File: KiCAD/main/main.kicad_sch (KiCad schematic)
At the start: 49 parts, among them J1 USB_C_Receptacle_USB2.0_14P, J2 Conn_Coaxial, J3 Conn_01x07_Socket, SW1 SW_SPDT, U1 SX1262IMLTRT, U2 TP4056-42-ESOP8, U3 BGS12P2L, U4 ESP32-S3-MINI-1, U6 MIC5219-3.3YMM, U7 CH340X

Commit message: added a huge schematic overhaul
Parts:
- removed H1, H2: MountingHole_Pad, MountingHole:MountingHole_2.2mm_M2_DIN965_Pad_TopBottom, symbol Mechanical:MountingHole_Pad
- removed TP5, TP6, TP7, TP8: TestPoint, TestPoint:TestPoint_Pad_1.5x1.5mm, symbol Connector:TestPoint
- added C8: 0.1uF, symbol Device:C
- added D3: WS2812B, LED_SMD:LED_WS2812B_PLCC4_5.0x5.0mm_P3.2mm, symbol LED:WS2812B
- added J4: Micro_SD_Card, customlib:SIM-SMD_8P-1040310811, symbol Connector:Micro_SD_Card
- added R11, R12, R13, R14, R15, R16, R17, R3, R6, R8: 10K, Resistor_SMD:R_0603_1608Metric, symbol Device:R
- added R18: R, symbol Device:R
- added SW2, SW3, SW4, SW5, SW6: SW_Push, customlib:SW-SMD_4P-L3.5-W3.0-P1.50-LS4.7, symbol Switch:SW_Push
- C1, C2: LCSC Part # C15849 -> C77386
- R10, R4, R9: LCSC Part # C25804 -> C2961367
- U4: LCSC Part # (none) -> C2913206
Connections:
- net GND: now also C8.1, D3.3 (VSS), J4.6 (VSS), J4.SH (SHIELD), SW2.2, SW3.2, SW4.2, SW5.2, SW6.2
- net VCC: now also C8.2, J4.4 (VDD), R11.2, R12.2, R13.1, R14.1, R15.1, R16.1, R17.1, R3.2, R6.2, R8.2, SW2.1, SW3.1, SW4.1, SW5.1, SW6.1
- net UP: now reaches U4.12 (IO8)
- net UP: now also R3.1
- net RIGHT: now reaches U4.13 (IO9)
- net RIGHT: now also R6.1
- net SEL: now reaches U4.14 (IO10)
- net SEL: now also R8.1
- net LEFT: now reaches U4.15 (IO11)
- net LEFT: now also R11.1
- net DOWN: now reaches U4.16 (IO12)
- net DOWN: now also R12.1
- net NEOPXL_D: now reaches U4.17 (IO13)
- net NEOPXL_D: now also R18.2
- net 5V: now reaches C1.2, SW1.1 (A), U6.1 (EN), U6.2 (IN)
- net 5V: now also D3.1 (VDD)
- new net: D3.4 (DIN), R18.1
- new net CLK: J4.5 (CLK)
- new net CMD: J4.3 (CMD), R15.2
- new net DAT0: J4.7 (DAT0), R14.2
- new net DAT1: J4.8 (DAT1), R13.2
- new net DAT2: J4.1 (DAT2), R16.2
- new net DAT3/CD: J4.2 (DAT3/CD), R17.2
- no-connect marks 9 -> 10
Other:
- note added: "DPAD"
- note added: "JTAG Probing Points"
- note added: "LiPo Charging"
- note added: "LoRa Radio Interface"
- note added: "MCU"
- note added: "Main USB Connection (USB-C)"
- note added: "Neopixel"
- note added: "Power Supply"
- note added: "SPI Display connector"
- note added: "Sheet Annotations"
- note added: "Storage"
- note added: "USB to Serial Bridge"
- note removed: "DNP"
- moved on the sheet: BT1, C1, C10, C11, C12, C13, C14, C15, C16, C17, C18, C2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

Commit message: Rev 3 done!
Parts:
- removed R10, R8, R9: 10K, Resistor_SMD:R_0603_1608Metric, symbol Device:R
- removed SW2, SW3, SW5, SW6: SW_Push, customlib:SW-SMD_4P-L3.5-W3.0-P1.50-LS4.7, symbol Switch:SW_Push
- added C19, C20, C9: 0.1uF, Capacitor_SMD:C_0402_1005Metric, symbol Device:C
- added SW2: RotaryEncoder, customlib:HYCW01-4D-4P-DZ, symbol Device:RotaryEncoder
- C8: footprint (none) -> Capacitor_SMD:C_0402_1005Metric; LCSC Part # (none) -> C1525
- D3: LCSC Part # (none) -> C114586
- FL1: LCSC Part # (none) -> C7434807; now in the parts list
- J3: now left out of the parts list
- J4: LCSC Part # (none) -> C585350
- R18: value R -> 450R; footprint (none) -> Resistor_SMD:R_0402_1005Metric; LCSC Part # (none) -> C186129
- SW4: footprint customlib:SW-SMD_4P-L3.5-W3.0-P1.50-LS4.7 -> customlib:SW-TH_3P-L5.8_WSGT-3P-CC; LCSC Part # C49393608 -> C22386787
- U4: now in the parts list
- renumbered TP3 to TCK1, TP1 to TDI1, TP2 to TDO1, TP4 to TMS1
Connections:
- net GND: now also SW4.1, C19.1, C20.2, C9.1, SW2.C; no longer SW4.2
- net NEOPXL_D: now also U4.44 (IO46); no longer U4.17 (IO13)
- net SEL: now also SW4.2, U4.16 (IO12), C20.1; no longer U4.14 (IO10)
- net VCC: no longer C10.1, C14.2, C17.2, C18.2, C2.2, C3.2, C4.2, C6.1, C7.1, C8.2, J4.4 (VDD), R11.2, R12.2, R13.1, R14.1, R15.1, R16.1, R17.1, R3.2, R4.1, R6.2, SW4.1, U1.1 (VDD_IN), U1.10 (VBAT), U1.11 (VBAT_IO), U3.4 (VDD), U4.3 (3V3), U6.3 (OUT), U7.10 (V3), U7.7 (VCC)
- net ~{CHRG}: now also R11.1, U4.32 (IO36); no longer U4.20 (IO16)
- net ~{STDBY}: now also R12.1, U4.31 (IO35); no longer U4.21 (IO17)
- net 5V renamed +5V
- removed net DOWN: R12.1, U4.16 (IO12)
- net LEFT renamed ENC_PHS_A
- net ENC_PHS_A: now also R6.1, C9.2, SW2.A; no longer R11.1
- net RIGHT renamed SCL
- net SCL: no longer R6.1
- net UP renamed ENC_PHS_B
- net ENC_PHS_B: now also U4.14 (IO10), C19.2, SW2.B; no longer U4.12 (IO8)
- new net +3.3V: C10.1, C14.2, C17.2, C18.2, C2.2, C3.2, C4.2, C6.1, C7.1, C8.2, J4.4 (VDD), R11.2, R12.2, R13.1, R14.1, R15.1, R16.1, R17.1, R3.2, R4.1, R6.2, U1.1 (VDD_IN), U1.10 (VBAT), U1.11 (VBAT_IO), U3.4 (VDD), U4.3 (3V3), U6.3 (OUT), U7.10 (V3), U7.7 (VCC)
- new net PWR: U4.17 (IO13)
- new net SDA: U4.12 (IO8)
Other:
- note added: "Dial"
- note added: "I2C"
- note removed: "DPAD"
- moved on the sheet: BT1, C1, C10, C11, C12, C13, C14, C15, C16, C17, C18, C2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

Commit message: Brushing off dust
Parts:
- removed C20: 0.1uF, Capacitor_SMD:C_0402_1005Metric, symbol Device:C
- removed SW4: SW_Push, customlib:SW-TH_3P-L5.8_WSGT-3P-CC, symbol Switch:SW_Push
- added H1, H2, H3, H4: MountingHole_Pad_MP, MountingHole:MountingHole_2.5mm_Pad_TopBottom, symbol Mechanical:MountingHole_Pad_MP
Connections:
- net GND: now also H1.MP, H2.MP, H3.MP, H4.MP
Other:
- note added: "Mounting"
- note removed: "I2C"
- moved on the sheet: C19, C9, R3, R6, SW2

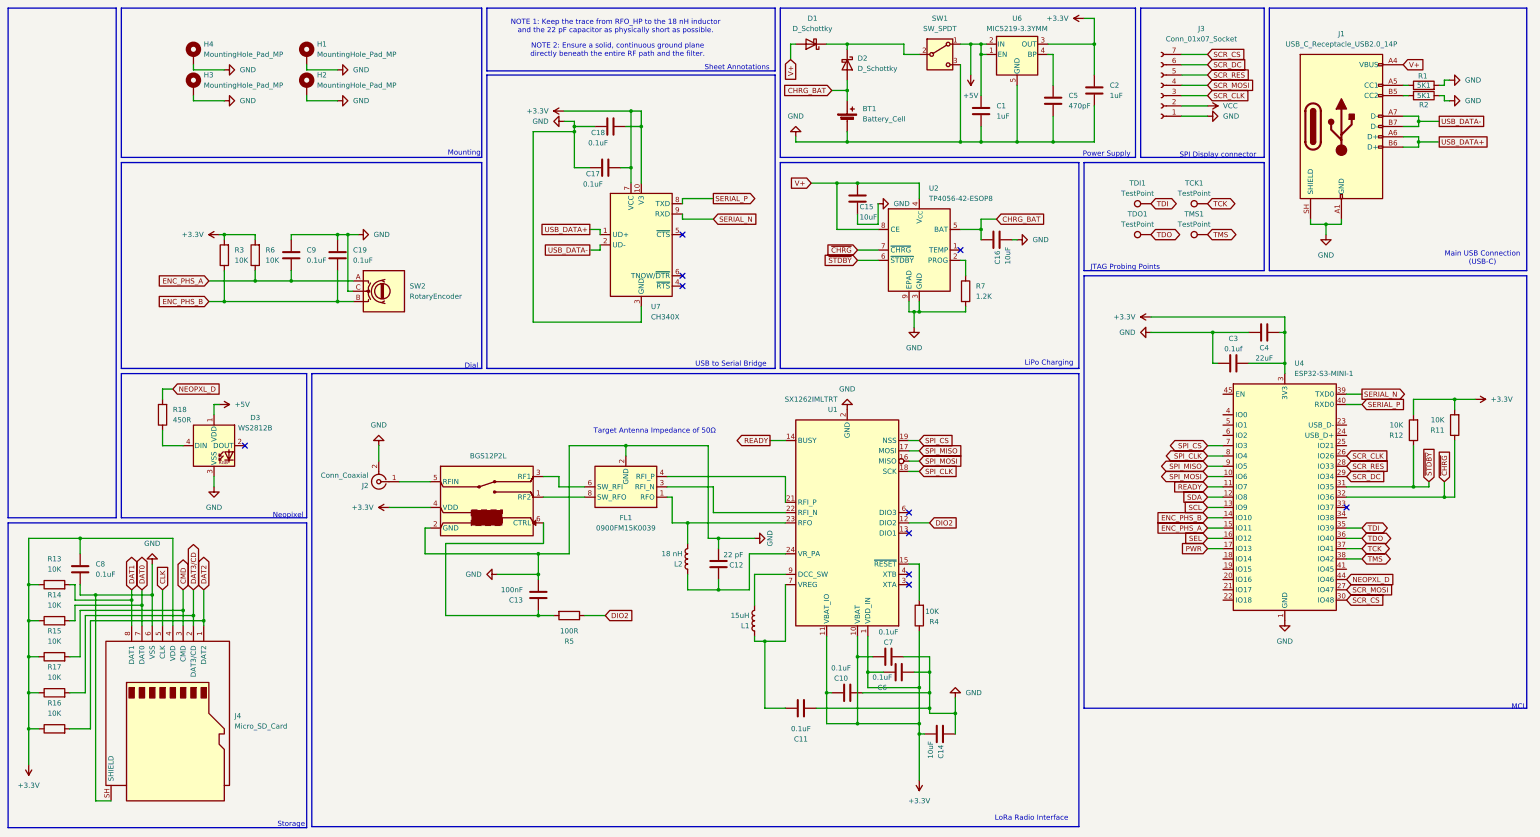
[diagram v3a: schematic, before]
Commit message: Replaced ESP-WROOM module with ESP32-S3 module for flexable usage and stocking
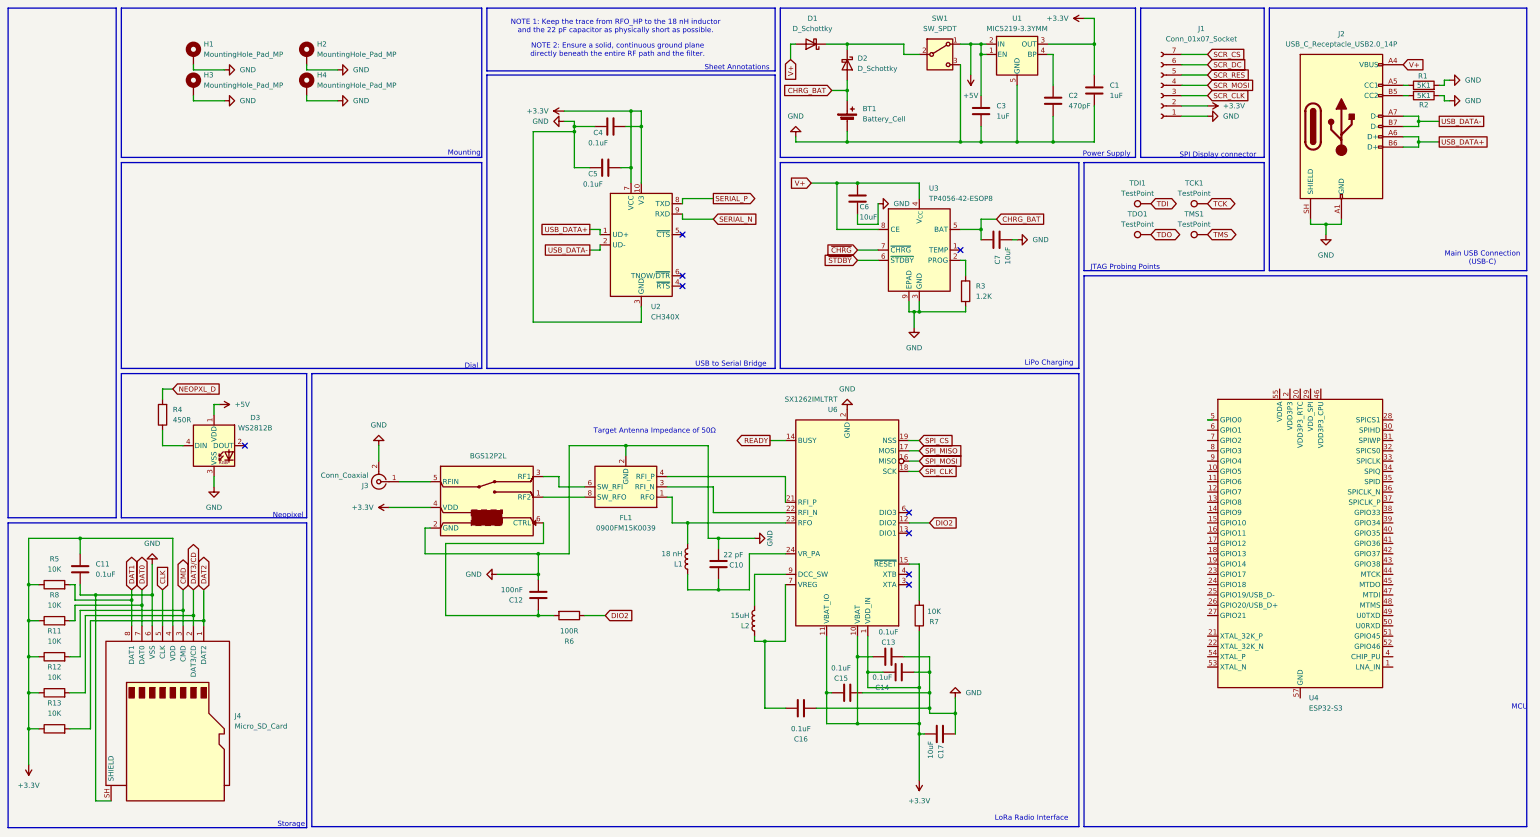
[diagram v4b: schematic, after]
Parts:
- removed C18, C19, C8, C9: 0.1uF, Capacitor_SMD:C_0402_1005Metric, symbol Device:C
- removed J1: USB_C_Receptacle_USB2.0_14P, Connector_USB:USB_C_Receptacle_GCT_USB4110, symbol Connector:USB_C_Receptacle_USB2.0_14P
- removed J2: Conn_Coaxial, Connector_Coaxial:SMA_Amphenol_132289_EdgeMount, symbol Connector:Conn_Coaxial
- removed J3: Conn_01x07_Socket, Connector_PinHeader_2.54mm:PinHeader_1x07_P2.54mm_Vertical, symbol Connector:Conn_01x07_Socket
- removed R14, R15, R16, R17: 10K, Resistor_SMD:R_0603_1608Metric, symbol Device:R
- removed R18: 450R, Resistor_SMD:R_0402_1005Metric, symbol Device:R
- removed SW2: RotaryEncoder, customlib:HYCW01-4D-4P-DZ, symbol Device:RotaryEncoder
- removed U1: SX1262IMLTRT, Package_DFN_QFN:QFN-24-1EP_4x4mm_P0.5mm_EP2.6x2.6mm, symbol RF:SX1262IMLTRT
- removed U2: TP4056-42-ESOP8, Package_SO:SOIC-8-1EP_3.9x4.9mm_P1.27mm_EP2.41x3.3mm_ThermalVias, symbol Battery_Management:TP4056-42-ESOP8
- removed U3: BGS12P2L, Package_LGA:Infineon_PG-TSNP-6-10_0.7x1.1mm_0.7x1.1mm_P0.4mm, symbol Personal:BGS12P2L
- removed U4: ESP32-S3-MINI-1, RF_Module:ESP32-S2-MINI-1, symbol RF_Module:ESP32-S3-MINI-1
- removed U6: MIC5219-3.3YMM, Package_SO:MSOP-8_3x3mm_P0.65mm, symbol Regulator_Linear:MIC5219-3.3YMM
- removed U7: CH340X, Package_SO:MSOP-10_3x3mm_P0.5mm, symbol Interface_USB:CH340X
- added J1: Conn_01x07_Socket, Connector_PinHeader_2.54mm:PinHeader_1x07_P2.54mm_Vertical, symbol Connector:Conn_01x07_Socket
- added J2: USB_C_Receptacle_USB2.0_14P, Connector_USB:USB_C_Receptacle_GCT_USB4110, symbol Connector:USB_C_Receptacle_USB2.0_14P
- added J3: Conn_Coaxial, Connector_Coaxial:SMA_Amphenol_132289_EdgeMount, symbol Connector:Conn_Coaxial
- added R8: 10K, Resistor_SMD:R_0603_1608Metric, symbol Device:R
- added U1: MIC5219-3.3YMM, Package_SO:MSOP-8_3x3mm_P0.65mm, symbol Regulator_Linear:MIC5219-3.3YMM
- added U2: CH340X, Package_SO:MSOP-10_3x3mm_P0.5mm, symbol Interface_USB:CH340X
- added U3: TP4056-42-ESOP8, Package_SO:SOIC-8-1EP_3.9x4.9mm_P1.27mm_EP2.41x3.3mm_ThermalVias, symbol Battery_Management:TP4056-42-ESOP8
- added U4: ESP32-S3, Package_DFN_QFN:QFN-56-1EP_7x7mm_P0.4mm_EP4x4mm, symbol MCU_Espressif:ESP32-S3
- added U5: BGS12P2L, Package_LGA:Infineon_PG-TSNP-6-10_0.7x1.1mm_0.7x1.1mm_P0.4mm, symbol Personal:BGS12P2L
- added U6: SX1262IMLTRT, Package_DFN_QFN:QFN-24-1EP_4x4mm_P0.5mm_EP2.6x2.6mm, symbol RF:SX1262IMLTRT
- C10: value 0.1uF -> 22 pF; footprint Capacitor_SMD:C_0402_1005Metric -> Capacitor_SMD:C_0603_1608Metric; LCSC Part # C1525 -> C1653
- C12: value 22 pF -> 100nF; footprint Capacitor_SMD:C_0603_1608Metric -> Capacitor_SMD:C_0402_1005Metric; LCSC Part # C1653 -> C1525
- C13: value 100nF -> 0.1uF
- C14, C15, C16: value 10uF -> 0.1uF; footprint Capacitor_SMD:C_0603_1608Metric -> Capacitor_SMD:C_0402_1005Metric; LCSC Part # C19702 -> C1525
- C17, C6, C7: value 0.1uF -> 10uF; footprint Capacitor_SMD:C_0402_1005Metric -> Capacitor_SMD:C_0603_1608Metric; LCSC Part # C1525 -> C19702
- C2: value 1uF -> 470pF; LCSC Part # C77386 -> C1620
- C3: value 0.1uf -> 1uF; footprint Capacitor_SMD:C_0402_1005Metric -> Capacitor_SMD:C_0603_1608Metric; LCSC Part # C1525 -> C77386
- C4: value 22uF -> 0.1uF; footprint Capacitor_SMD:C_0805_2012Metric -> Capacitor_SMD:C_0402_1005Metric; LCSC Part # C45783 -> C1525
- C5: value 470pF -> 0.1uF; footprint Capacitor_SMD:C_0603_1608Metric -> Capacitor_SMD:C_0402_1005Metric; LCSC Part # C1620 -> C1525
- L1: value 15uH -> 18 nH; footprint Inductor_SMD:L_0805_2012Metric -> Inductor_SMD:L_0603_1608Metric; LCSC Part # C383402 -> C19721138
- L2: value 18 nH -> 15uH; footprint Inductor_SMD:L_0603_1608Metric -> Inductor_SMD:L_0805_2012Metric; LCSC Part # C19721138 -> C383402
- R3: value 10K -> 1.2K; LCSC Part # C2961367 -> C22765
- R4: value 10K -> 450R; footprint Resistor_SMD:R_0603_1608Metric -> Resistor_SMD:R_0402_1005Metric; LCSC Part # C2961367 -> C186129
- R5: value 100R -> 10K; footprint Resistor_SMD:R_0402_1005Metric -> Resistor_SMD:R_0603_1608Metric; LCSC Part # C25076 -> C2961367
- R6: value 10K -> 100R; footprint Resistor_SMD:R_0603_1608Metric -> Resistor_SMD:R_0402_1005Metric; LCSC Part # C2961367 -> C25076
- R7: value 1.2K -> 10K; LCSC Part # C22765 -> C2961367
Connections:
- net ENC_PHS_A is gone; now on net DIO2: R6.1
- net +3.3V: now also C1.2, C11.2, C13.1, C14.1, C15.1, C5.2, R11.1, R12.1, R5.1, R7.1, J1.2 (Pin_2), R8.1, U1.3 (OUT), U2.10 (V3), U2.7 (VCC), U5.4 (VDD), U6.1 (VDD_IN), U6.10 (VBAT), U6.11 (VBAT_IO); no longer C10.1, C14.2, C2.2, C3.2, C6.1, C7.1, R11.2, R12.2, R3.2, R4.1, R6.2
- net +5V: now also C3.2, U1.1 (EN), U1.2 (IN); no longer C1.2
- net CHRG_BAT: now also C7.2, U3.5 (BAT); no longer C16.2
- net CMD: now also R11.2
- net DAT0: now also R8.2
- net DAT1: now also R5.2; no longer R13.2
- net DAT2: now also R13.2
- net DAT3/CD: now also R12.2
- net DIO2: now also U6.12 (DIO2); no longer R5.1
- net GND: now also C14.2, C2.2, C5.1, C7.1, R3.2, J1.1 (Pin_1), J2.A1 (GND), J2.A12 (GND), J2.B1 (GND), J2.B12 (GND), J2.SH (SHIELD), J3.2 (Ext), U1.5 (GND), U1.6 (GND), U1.7 (GND), U1.8 (GND), U2.3 (GND), U3.3 (GND), U3.9 (EPAD), U5.2 (GND), U6.2 (GND), U6.20 (GND), U6.25 (GND), U6.5 (GND), U6.8 (GND); no longer C14.1, C2.1, C5.2, C7.2, R7.2
- net NEOPXL_D: now also R4.2
- net READY: now also U6.14 (BUSY)
- net SCR_CLK: now also J1.3 (Pin_3)
- net SCR_CS: now also J1.7 (Pin_7)
- net SCR_DC: now also J1.6 (Pin_6)
- net SCR_MOSI: now also J1.4 (Pin_4)
- net SCR_RES: now also J1.5 (Pin_5)
- net SERIAL_N: now also U2.9 (RXD)
- net SERIAL_P: now also U2.8 (TXD)
- net SPI_CLK: now also U6.18 (SCK)
- net SPI_CS: now also U6.19 (NSS)
- net SPI_MISO: now also U6.17 (MOSI)
- net SPI_MOSI: now also U6.16 (MISO)
- net USB_DATA+: now also J2.A6 (D+), J2.B6 (D+), U2.1 (UD+)
- net USB_DATA-: now also J2.A7 (D-), J2.B7 (D-), U2.2 (UD-)
- net V+: now also C6.1, J2.A4 (VBUS), J2.A9 (VBUS), J2.B4 (VBUS), J2.B9 (VBUS), U3.4 (V_{CC}), U3.8 (CE); no longer C15.1
- net ~{CHRG}: now also U3.7 (~{CHRG}); no longer R11.1
- net ~{STDBY}: now also U3.6 (~{STDBY}); no longer R12.1
- net at C12.1: now also R6.2, U5.6 (CTRL); no longer L2.1
- net at FL1.8 (SW_RFO): now also U5.1 (RF2)
- net at FL1.6 (SW_RFI): now also U5.3 (RF1)
- net at L1.1: now also C10.1, U6.24 (VR_PA); no longer C11.2
- net at L1.2: now also FL1.1 (RFO), U6.23 (RFO)
- net at R1.1: now also J2.A5 (CC1)
- net at R2.2: now also J2.B5 (CC2)
- net at FL1.4 (RFI_P): now also U6.21 (RFI_P)
- net at FL1.3 (RFI_N): now also U6.22 (RFI_N)
- net at L2.2: now also U6.9 (DCC_SW); no longer FL1.1 (RFO)
- net at D3.4 (DIN): now also R4.1
- net ENC_PHS_B: no longer names the net of R3.1
- net ENC_PHS_B: now also U3.2 (PROG)
- new net: C2.1, U1.4 (BP)
- new net: R7.2, U6.15 (~{RESET})
- new net: C16.2, L2.1, U6.7 (VREG)
- new net: J3.1 (In), U5.5 (RFIN)
- new net: U4.2 (VDD3P3), U4.3 (VDD3P3)
- new net: U4.55 (VDDA), U4.56 (VDDA)
- no-connect marks 10 -> 9
